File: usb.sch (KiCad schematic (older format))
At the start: 17 parts, among them J7 USB_C_Receptacle_USB2.0, J8 USB_B_Micro, U3 MIC2025

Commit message: Start the routing
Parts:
- J8: symbol Connector:USB_B_Micro -> Connector:USB_OTG
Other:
- moved on the sheet: R29, R30
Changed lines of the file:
@@
 $EndDescr
 $Comp
-L Connector:USB_B_Micro J?
+L Connector:USB_OTG J?
 U 1 1 5CD3A60B
 P 4200 2450
@@
 Wire Wire Line
 	4550 2250 4550 2200
-$Comp
-L power:VBUS #PWR0144
-U 1 1 5CD3A61E
-P 4550 2200
-F 0 "#PWR0144" H 4550 2050 50  0001 C CNN
-F 1 "VBUS" H 4565 2373 50  0000 C CNN
-F 2 "" H 4550 2200 50  0001 C CNN
-F 3 "" H 4550 2200 50  0001 C CNN
-	1    4550 2200
-	1    0    0    -1
-$EndComp
 Wire Wire Line
 	4550 2250 5100 2250
@@
 	4750 4750 4800 4750
 Connection ~ 4750 4750
-Wire Wire Line
-	4700 4050 4750 4050
-Text Label 4750 4050 0    50   ~ 0
-B_VBUS
 $Comp
 L Power_Management_Extra:MIC2025 U3
@@
 Text HLabel 8100 4050 2    50   Output ~ 0
 B_OVERCURR
-Text Label 8100 4250 0    50   ~ 0
-B_VBUS
 $Comp
 L Device:R_Small R29
 U 1 1 5CD3A702
-P 4900 4250
-F 0 "R29" V 4850 4150 50  0000 R CNN
-F 1 "5.1K" V 4850 4350 50  0000 L CNN
-F 2 "Resistor_SMD:R_0603_1608Metric" H 4900 4250 50  0001 C CNN
-F 3 "~" H 4900 4250 50  0001 C CNN
-	1    4900 4250
-	0    1    1    0
-$EndComp
-Wire Wire Line
-	4700 4250 4800 4250
+P 4950 4250
+F 0 "R29" V 4900 4150 50  0000 R CNN
+F 1 "5.1K" V 4900 4350 50  0000 L CNN
+F 2 "Resistor_SMD:R_0603_1608Metric" H 4950 4250 50  0001 C CNN
+F 3 "~" H 4950 4250 50  0001 C CNN
+	1    4950 4250
+	0    1    1    0
+$EndComp
+Wire Wire Line
+	4700 4250 4850 4250
 $Comp
 L Device:R_Small R30
 U 1 1 5CD3A709
-P 4900 4350
-F 0 "R30" V 4850 4250 50  0000 R CNN
-F 1 "5.1K" V 4850 4450 50  0000 L CNN
-F 2 "Resistor_SMD:R_0603_1608Metric" H 4900 4350 50  0001 C CNN
-F 3 "~" H 4900 4350 50  0001 C CNN
-	1    4900 4350
-	0    1    1    0
-$EndComp
-Wire Wire Line
-	4700 4350 4800 4350
-Wire Wire Line
-	5000 4250 5200 4250
-Wire Wire Line
-	5000 4350 5200 4350
+P 4950 4350
+F 0 "R30" V 4900 4250 50  0000 R CNN
+F 1 "5.1K" V 4900 4450 50  0000 L CNN
+F 2 "Resistor_SMD:R_0603_1608Metric" H 4950 4350 50  0001 C CNN
+F 3 "~" H 4950 4350 50  0001 C CNN
+	1    4950 4350
+	0    1    1    0
+$EndComp
+Wire Wire Line
+	4700 4350 4850 4350
+Wire Wire Line
+	5050 4250 5250 4250
+Wire Wire Line
+	5050 4350 5250 4350
 $Comp
 L power:+3.3V #PWR0146
 U 1 1 5CD3A712
-P 5200 4250
-F 0 "#PWR0146" H 5200 4100 50  0001 C CNN
-F 1 "+3.3V" V 5200 4400 50  0000 L CNN
-F 2 "" H 5200 4250 50  0001 C CNN
-F 3 "" H 5200 4250 50  0001 C CNN
-	1    5200 4250
+P 5250 4250
+F 0 "#PWR0146" H 5250 4100 50  0001 C CNN
+F 1 "+3.3V" V 5250 4400 50  0000 L CNN
+F 2 "" H 5250 4250 50  0001 C CNN
+F 3 "" H 5250 4250 50  0001 C CNN
+	1    5250 4250
 	0    1    1    0
 $EndComp
@@
 L power:+3.3V #PWR0147
 U 1 1 5CD3A718
-P 5200 4350
-F 0 "#PWR0147" H 5200 4200 50  0001 C CNN
-F 1 "+3.3V" V 5200 4500 50  0000 L CNN
-F 2 "" H 5200 4350 50  0001 C CNN
-F 3 "" H 5200 4350 50  0001 C CNN
-	1    5200 4350
+P 5250 4350
+F 0 "#PWR0147" H 5250 4200 50  0001 C CNN
+F 1 "+3.3V" V 5250 4500 50  0000 L CNN
+F 2 "" H 5250 4350 50  0001 C CNN
+F 3 "" H 5250 4350 50  0001 C CNN
+	1    5250 4350
 	0    1    1    0
 $EndComp
@@
 Text HLabel 4550 2550 2    50   BiDi ~ 0
 A_D-
+Wire Wire Line
+	4700 4050 4750 4050
+Text Label 4750 4050 0    50   ~ 0
+B_VBUS
+Text Label 8100 4250 0    50   ~ 0
+B_VBUS
+$Comp
+L power:VBUS #PWR0144
+U 1 1 5CD3A61E
+P 4550 2200
+F 0 "#PWR0144" H 4550 2050 50  0001 C CNN
+F 1 "VBUS" H 4565 2373 50  0000 C CNN
+F 2 "" H 4550 2200 50  0001 C CNN
+F 3 "" H 4550 2200 50  0001 C CNN
+	1    4550 2200
+	1    0    0    -1
+$EndComp
 $EndSCHEMATC

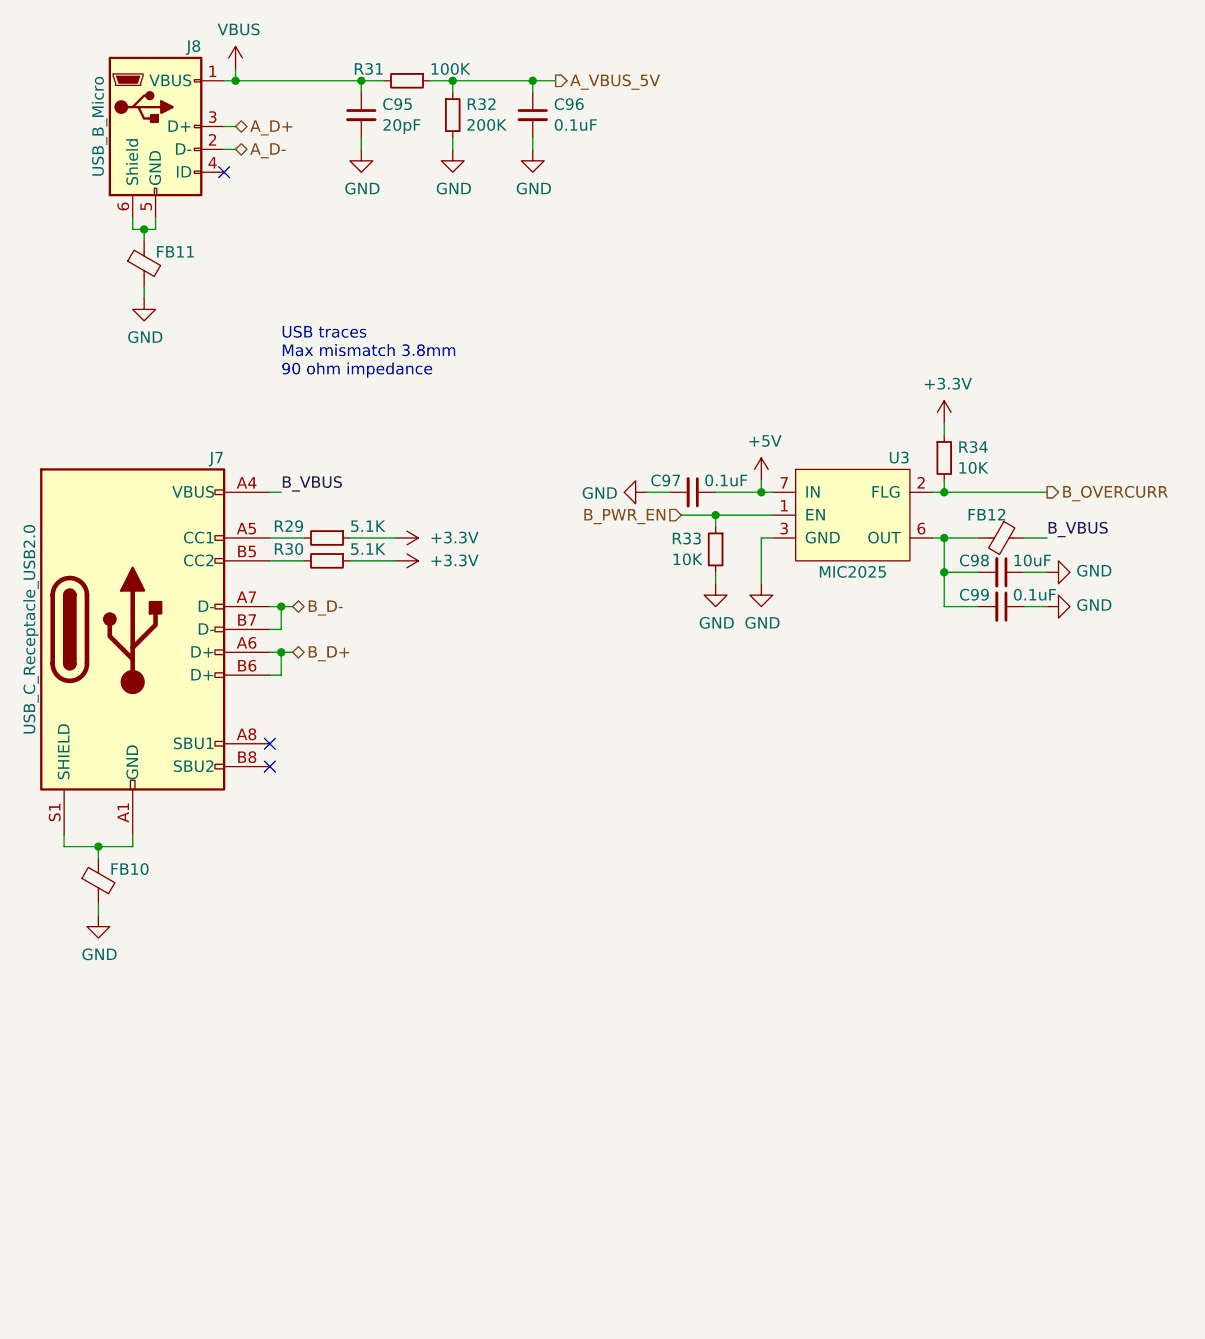
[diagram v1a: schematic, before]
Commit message: More routing, 165 unconnected left
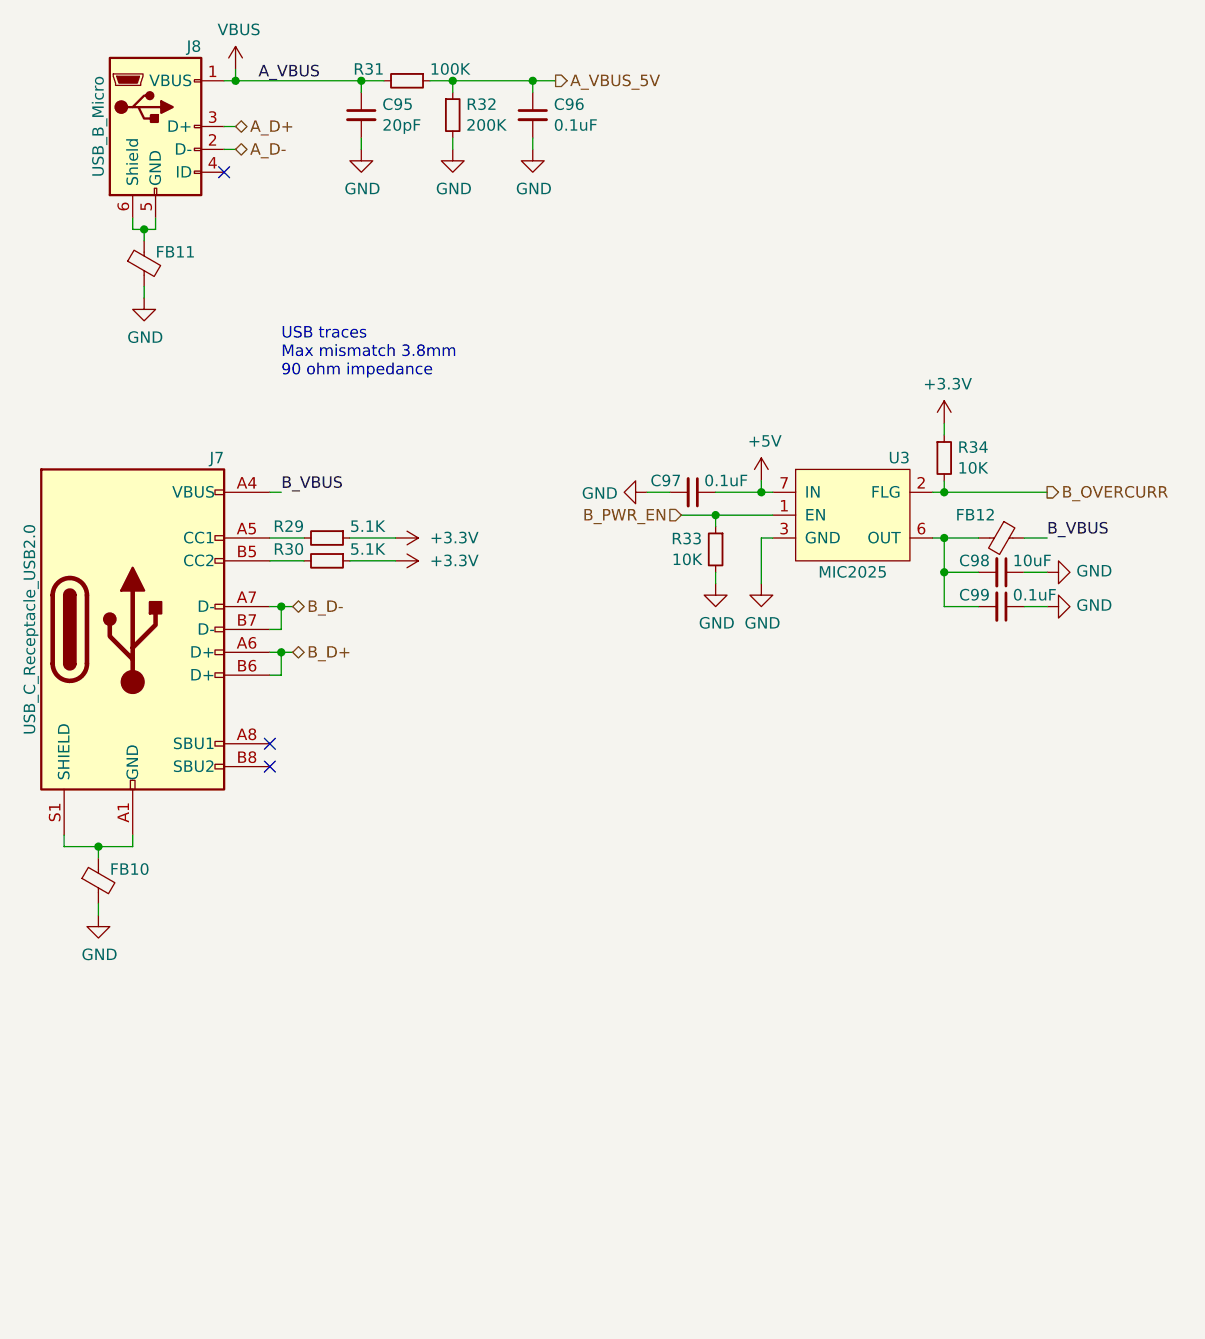
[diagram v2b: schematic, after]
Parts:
- FB10, FB11, FB12: value 10R 1A -> BLM18PG300SN1D
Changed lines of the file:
@@
 Wire Wire Line
 	4550 2250 4550 2200
-Wire Wire Line
-	4550 2250 5100 2250
-Connection ~ 4550 2250
 $Comp
 L Device:R_Small R31
@@
 Wire Wire Line
 	5100 2250 5100 2300
-Connection ~ 5100 2250
 Wire Wire Line
 	5100 2250 5200 2250
@@
 AR Path="/5CCDEAD5/5CD3A65E" Ref="FB11"  Part="1"
 F 0 "FB11" H 4200 3100 50  0000 L CNN
-F 1 "10R 1A" V 4296 3050 50  0001 C CNN
+F 1 "BLM18PG300SN1D" V 4296 3050 50  0001 C CNN
 F 2 "Inductor_SMD:L_0603_1608Metric" V 4080 3050 50  0001 C CNN
 F 3 "~" H 4150 3050 50  0001 C CNN
@@
 AR Path="/5CCDEAD5/5CD3A674" Ref="FB10"  Part="1"
 F 0 "FB10" H 4000 5800 50  0000 L CNN
-F 1 "10R 1A" V 4096 5750 50  0001 C CNN
+F 1 "BLM18PG300SN1D" V 4096 5750 50  0001 C CNN
 F 2 "Inductor_SMD:L_0603_1608Metric" V 3880 5750 50  0001 C CNN
 F 3 "~" H 3950 5750 50  0001 C CNN
@@
 AR Path="/5CD3A6C6" Ref="FB?"  Part="1"
 AR Path="/5CCDEAD5/5CD3A6C6" Ref="FB12"  Part="1"
-F 0 "FB12" V 7800 4100 50  0000 L CNN
-F 1 "10R 1A" V 8046 4250 50  0001 C CNN
+F 0 "FB12" V 7800 4050 50  0000 L CNN
+F 1 "BLM18PG300SN1D" V 8046 4250 50  0001 C CNN
 F 2 "Inductor_SMD:L_0603_1608Metric" V 7830 4250 50  0001 C CNN
 F 3 "~" H 7900 4250 50  0001 C CNN
@@
 Wire Wire Line
 	8000 4550 8100 4550
-Wire Wire Line
-	8000 4250 8100 4250
 $Comp
 L power:GND #PWR0155
@@
 Text HLabel 4550 2550 2    50   BiDi ~ 0
 A_D-
+Text Label 8100 4250 0    50   ~ 0
+B_VBUS
+Text Label 4650 2250 0    50   ~ 0
+A_VBUS
+Wire Wire Line
+	8000 4250 8100 4250
 Wire Wire Line
 	4700 4050 4750 4050
+Connection ~ 5100 2250
+Connection ~ 4550 2250
+Wire Wire Line
+	4550 2250 5100 2250
 Text Label 4750 4050 0    50   ~ 0
 B_VBUS
-Text Label 8100 4250 0    50   ~ 0
-B_VBUS
-$Comp
+$Comp

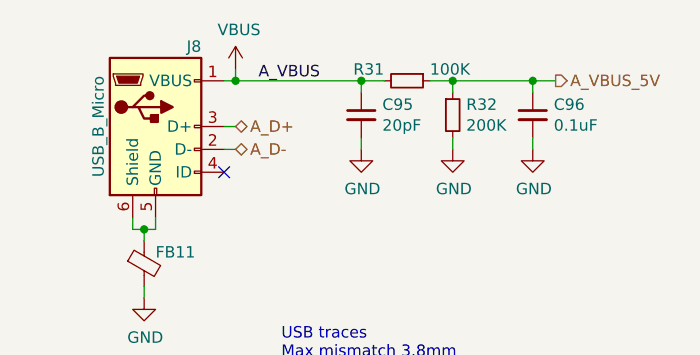
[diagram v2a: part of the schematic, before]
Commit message: Fix USB bug by updating symbols lib
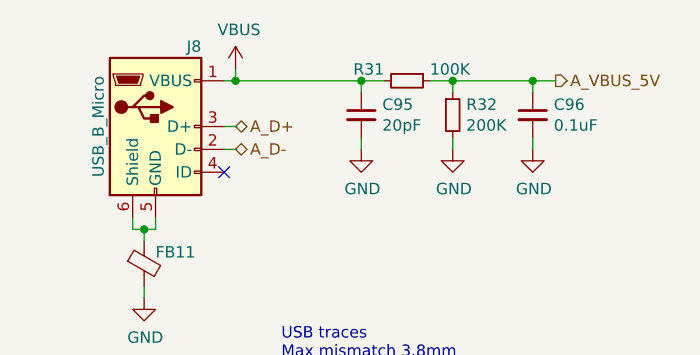
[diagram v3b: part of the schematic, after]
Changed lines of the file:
@@
 U 1 1 5CD3A66C
 P 4100 4650
+AR Path="/5CD3A66C" Ref="J7"  Part="1"
+AR Path="/5CCDEAD5/5CD3A66C" Ref="J7"  Part="1"
 F 0 "J7" H 4500 5400 50  0000 R CNN
 F 1 "USB_C_Receptacle_USB2.0" V 3650 4650 50  0000 C CNN
@@
 Text Label 8100 4250 0    50   ~ 0
 B_VBUS
-Text Label 4650 2250 0    50   ~ 0
-A_VBUS
 Wire Wire Line
 	8000 4250 8100 4250

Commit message: Almost routed, just 2 unconnected left
Hahahahahah HahahaHhahaHAHAhahahHAHAHAHhahah
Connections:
- net A_GND: now reaches FB11.1, J8.5 (GND), J8.6 (Shield)
- net B_GND: now reaches FB10.1, J7.A1 (GND), J7.A12 (GND), J7.B1 (GND), J7.B12 (GND), J7.S1 (SHIELD)
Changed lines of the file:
@@
 	1    0    0    -1
 $EndComp
+Text Label 4100 5600 0    50   ~ 0
+B_GND
+Text Label 4200 2900 0    50   ~ 0
+A_GND
+$Comp
+L power:VBUS #PWR0165
+U 1 1 5C20E108
+P 5300 7350
+F 0 "#PWR0165" H 5300 7200 50  0001 C CNN
+F 1 "VBUS" H 5315 7523 50  0000 C CNN
+F 2 "" H 5300 7350 50  0001 C CNN
+F 3 "" H 5300 7350 50  0001 C CNN
+	1    5300 7350
+	1    0    0    -1
+$EndComp
+Wire Wire Line
+	5300 7350 5300 7450
+$Comp
+L power:PWR_FLAG #FLG0101
+U 1 1 5C20F4D5
+P 5300 7450
+F 0 "#FLG0101" H 5300 7525 50  0001 C CNN
+F 1 "PWR_FLAG" H 5300 7623 50  0000 C CNN
+F 2 "" H 5300 7450 50  0001 C CNN
+F 3 "~" H 5300 7450 50  0001 C CNN
+	1    5300 7450
+	-1   0    0    1
+$EndComp
+Text Label 5750 7250 0    50   ~ 0
+B_VBUS
+Wire Wire Line
+	5750 7250 5750 7450
+$Comp
+L power:PWR_FLAG #FLG0102
+U 1 1 5C211A50
+P 5750 7450
+F 0 "#FLG0102" H 5750 7525 50  0001 C CNN
+F 1 "PWR_FLAG" H 5750 7623 50  0000 C CNN
+F 2 "" H 5750 7450 50  0001 C CNN
+F 3 "~" H 5750 7450 50  0001 C CNN
+	1    5750 7450
+	-1   0    0    1
+$EndComp
+Text Label 6200 7250 0    50   ~ 0
+A_GND
+Text Label 6650 7250 0    50   ~ 0
+B_GND
+Wire Wire Line
+	6200 7250 6200 7450
+Wire Wire Line
+	6650 7250 6650 7450
+$Comp
+L power:PWR_FLAG #FLG0103
+U 1 1 5C21777A
+P 6200 7450
+F 0 "#FLG0103" H 6200 7525 50  0001 C CNN
+F 1 "PWR_FLAG" H 6200 7623 50  0000 C CNN
+F 2 "" H 6200 7450 50  0001 C CNN
+F 3 "~" H 6200 7450 50  0001 C CNN
+	1    6200 7450
+	-1   0    0    1
+$EndComp
+$Comp
+L power:PWR_FLAG #FLG0104
+U 1 1 5C2178C4
+P 6650 7450
+F 0 "#FLG0104" H 6650 7525 50  0001 C CNN
+F 1 "PWR_FLAG" H 6650 7623 50  0000 C CNN
+F 2 "" H 6650 7450 50  0001 C CNN
+F 3 "~" H 6650 7450 50  0001 C CNN
+	1    6650 7450
+	-1   0    0    1
+$EndComp
 $EndSCHEMATC
